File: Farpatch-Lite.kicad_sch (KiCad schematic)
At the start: 33 parts, among them J1 Program Header, J2 SWD Connector, SW1 Pushbutton 2.1x1.6mm, SW2 Pushbutton 2.1x1.6mm, U1 ‎ESP32-D0WD-V3‎, U2 Flash 32 Mb SPI, Y1 Crystal 40MHz

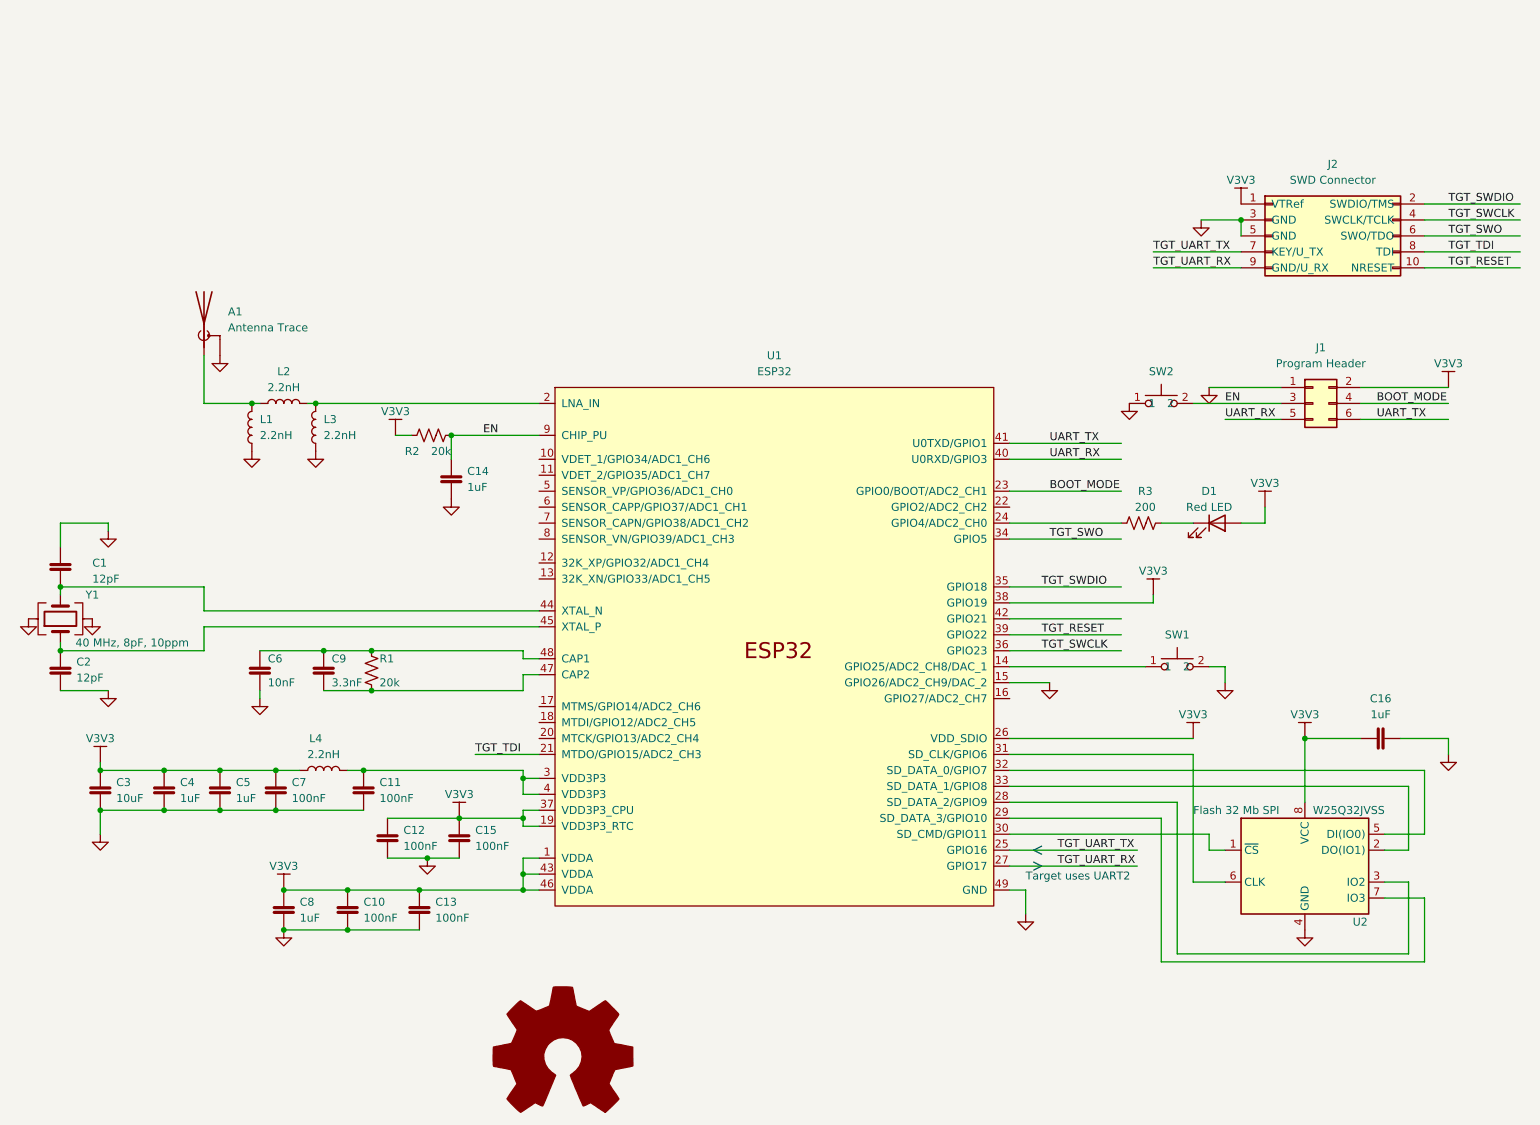
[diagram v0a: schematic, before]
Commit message: farpatch: finish layout and update README
Signed-off-by: Sean Cross <sean@xobs.io>
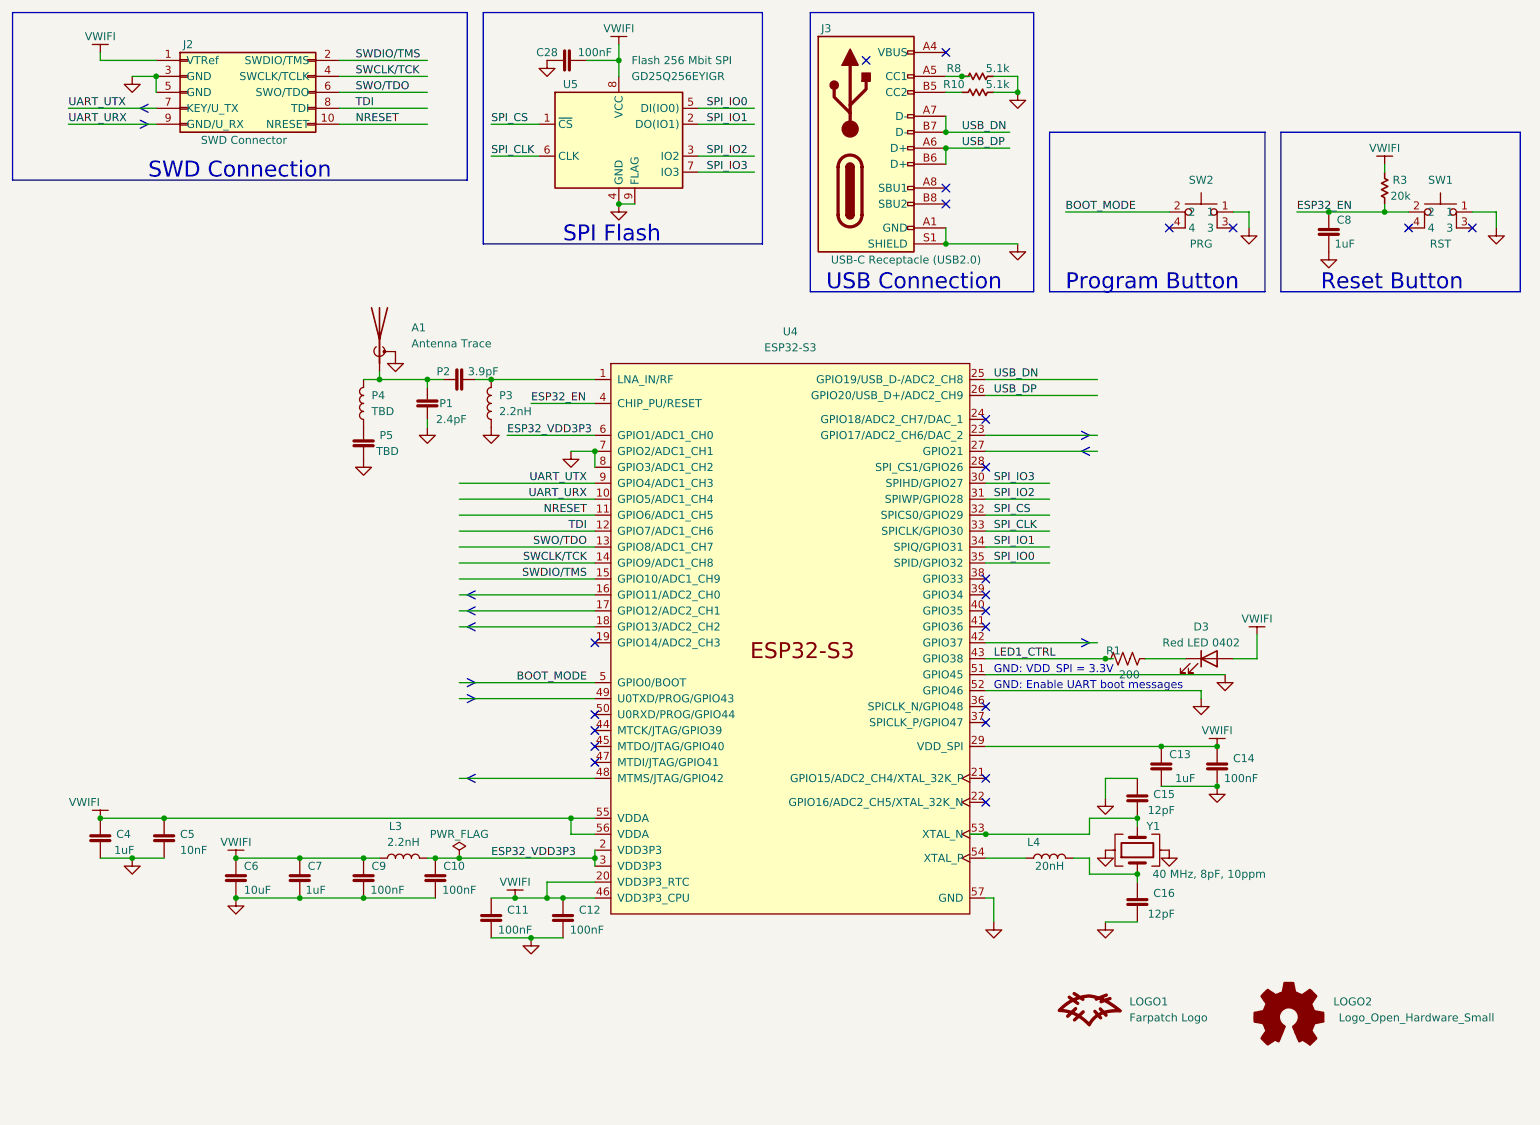
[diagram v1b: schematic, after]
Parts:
- removed C1, C2: Cap 12pF 0402, Capacitor_SMD:C_0402_1005Metric, symbol Farpatch-Lite:Cap 12pF 0402
- removed C13, C15, C7: Cap 100nF 0402, Capacitor_SMD:C_0402_1005Metric, symbol Farpatch-Lite:Cap 100nF 0402
- removed C14, C16, C5: Cap 1uF 0402, Capacitor_SMD:C_0402_1005Metric, symbol Farpatch-Lite:Cap 1uF 0402
- removed C3: Cap 10uF 0402, Capacitor_SMD:C_0402_1005Metric, symbol Farpatch-Lite:Cap 10uF 0402
- removed C6: Cap 10nF 0402, Capacitor_SMD:C_0402_1005Metric, symbol Farpatch-Lite:Cap 10nF 0402
- removed C9: Cap 3.3nF 0402, Capacitor_SMD:C_0402_1005Metric, symbol Farpatch-Lite:Cap 3.3nF 0402
- removed D1: Red LED, Farpatch-Lite:LED_0402_1005Metric, symbol Farpatch-Lite:Red LED
- removed J1: Program Header, Farpatch-Lite:PinHeader_2x03_P2.54mm_Vertical, symbol Farpatch-Lite:Program Header
- removed L1, L2, L3, L4: Ind 2.2nH 0402, Inductor_SMD:L_0402_1005Metric, symbol Farpatch-Lite:Ind 2.2nH 0402
- removed LOGO1: Logo_Open_Hardware_Large, Symbol:OSHW-Logo_5.7x6mm_SilkScreen, symbol Graphic:Logo_Open_Hardware_Large
- removed R1, R2: Res 20k 0402, Resistor_SMD:R_0402_1005Metric, symbol Farpatch-Lite:Res 20k 0402
- removed R3: Res 200 0402, Resistor_SMD:R_0402_1005Metric, symbol Farpatch-Lite:Res 200 0402
- removed SW1, SW2: Pushbutton 2.1x1.6mm, Farpatch-Lite:Pushbutton-2.1x1.6mm, symbol Farpatch-Lite:Pushbutton 2.1x1.6mm
- removed U1: ‎ESP32-D0WD-V3‎, Farpatch-Lite:QFN-48-1EP_5x5mm_P0.35mm_EP3.7x3.7mm_ThermalVias, symbol Farpatch-Lite:‎ESP32-D0WD-V3‎
- removed U2: Flash 32 Mb SPI, Farpatch-Lite:SOIC-8_5.23x5.23mm_P1.27mm, symbol Farpatch-Lite:Flash 32 Mb SPI
- added C13, C7: Cap 1uF 0402, Capacitor_SMD:C_0402_1005Metric, symbol Farpatch-Lite:Cap 1uF 0402
- added C14, C28, C9: Cap 100nF 0402, Capacitor_SMD:C_0402_1005Metric, symbol Farpatch-Lite:Cap 100nF 0402
- added C15, C16: Cap 12pF 0402, Capacitor_SMD:C_0402_1005Metric, symbol Farpatch-Lite:Cap 12pF 0402
- added C5: Cap 10nF 0402, Capacitor_SMD:C_0402_1005Metric, symbol Farpatch:Cap 10nF 0402
- added C6: Cap 10uF 0603, Capacitor_SMD:C_0603_1608Metric, symbol Farpatch:Cap 10uF 0603
- added D3: Red LED 0402, Farpatch-Lite:LED_0402_1005Metric, symbol Farpatch:Red LED 0402
- added J3: USB-C Receptacle (USB2.0), Farpatch-Lite:USB_C_Receptacle_HRO_TYPE-C-31-M-12, symbol Farpatch-Lite:USB-C Receptacle (USB2.0)
- added L3: L 2.2nH 0402, Inductor_SMD:L_0402_1005Metric, symbol Farpatch:L 2.2nH 0402
- added L4: L 20nH 0402, Inductor_SMD:L_0402_1005Metric, symbol Farpatch-Lite:L 20nH 0402
- added LOGO1: Farpatch Logo, Farpatch-Lite:Farpatch Logo, symbol Farpatch-Lite:Farpatch Logo
- added LOGO2: Logo_Open_Hardware_Small, Symbol:OSHW-Logo_5.7x6mm_SilkScreen, symbol Graphic:Logo_Open_Hardware_Small
- added P1: Cap 2.4pF 0402, Capacitor_SMD:C_0402_1005Metric, symbol Farpatch:Cap 2.4pF 0402
- added P2, P5: Cap 3.9pF 0402, Capacitor_SMD:C_0402_1005Metric, symbol Farpatch:Cap 3.9pF 0402
- added P3, P4: L 2.7 nH 0402, Inductor_SMD:L_0402_1005Metric, symbol Farpatch:L 2.7 nH 0402
- added R1: Res 200 0402, Resistor_SMD:R_0402_1005Metric, symbol Farpatch-Lite:Res 200 0402
- added R10, R8: R 5.1k 0402, Resistor_SMD:R_0402_1005Metric, symbol Farpatch:R 5.1k 0402
- added R3: Res 20k 0402, Resistor_SMD:R_0402_1005Metric, symbol Farpatch:R 20k 0402
- added SW1, SW2: Pushbutton 4.2x3.2mm 250gf, Farpatch-Lite:SW_SPST_PTS810, symbol Farpatch:Pushbutton 4.2x3.2mm 250gf
- added U4: ESP32-S3, Farpatch-Lite:QFN-56-1EP_7x7mm_P0.4mm_EP5.6x5.6mm_ThermalVias, symbol Farpatch-Lite:ESP32-S3
- added U5: Flash 256 Mbit SPI, Farpatch-Lite:WSON-8_8x6mm_P1.27mm, symbol Farpatch-Lite:Flash 256 Mbit SPI
- C11, C4: now in the parts list
- J2: footprint Farpatch-Lite:PinHeader_2x05_P1.27mm_Vertical_SMD -> Connector_PinHeader_1.27mm:PinHeader_2x05_P1.27mm_Vertical; Digikey (none) -> https://www.digikey.com/en/products/detail/cnc-tech/3220-10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
- Y1: value Crystal 40MHz -> Crystal 40MHz 2016
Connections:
- net BOOT_MODE: now also SW2.2, U4.5 (GPIO0/BOOT)
- net GND: now also C13.2, C14.2, C15.1, C16.2, C28.1, C5.2, C6.2, C7.2, C9.2, J3.A1 (GND), J3.A12 (GND), J3.B1 (GND), J3.B12 (GND), J3.S1 (SHIELD), P1.1, P3.1, P5.1, R10.2, R8.2, SW1.1, SW2.1, U4.51 (GPIO45), U4.52 (GPIO46), U4.57 (GND), U4.7 (GPIO2/ADC1_CH1), U4.8 (GPIO3/ADC1_CH2), U5.4 (GND), U5.9 (FLAG)
- net at Y1.1: now also C16.1, L4.2
- net at Y1.3: now also C15.2, U4.53 (XTAL_N)
- net VWIFI: now reaches C11.1
- net VWIFI: now also C12.1, C4.1, J2.1 (VTRef), C13.1, C14.1, C28.2, C5.1, C6.1, C7.1, C9.1, D3.2 (A), L3.1, R3.2, U4.20 (VDD3P3_RTC), U4.29 (VDD_SPI), U4.46 (VDD3P3_CPU), U4.55 (VDDA), U4.56 (VDDA), U5.8 (VCC)
- net at A1.1 (A): now also P1.2, P2.1, P4.2
- net TGT_RESET renamed NRESET
- net NRESET: now also U4.11 (GPIO6/ADC1_CH5)
- net TGT_SWCLK renamed SWCLK/TCK
- net SWCLK/TCK: now also U4.14 (GPIO9/ADC1_CH8)
- net TGT_SWDIO renamed SWDIO/TMS
- net SWDIO/TMS: now also U4.15 (GPIO10/ADC1_CH9)
- net TGT_SWO renamed SWO/TDO
- net SWO/TDO: now also U4.13 (GPIO8/ADC1_CH7)
- net TGT_TDI renamed TDI
- net TDI: now also U4.12 (GPIO7/ADC1_CH6)
- net TGT_UART_RX renamed UART_URX
- net UART_URX: now also U4.10 (GPIO5/ADC1_CH4)
- net TGT_UART_TX renamed UART_UTX
- net UART_UTX: now also U4.9 (GPIO4/ADC1_CH3)
- removed net V3V3: C10.1, C12.1, C4.1, C8.1, J2.1 (VTRef)
- new net: P2.2, P3.2, U4.1 (LNA_IN/RF)
- new net: D3.1 (K), R1.2
- new net: J3.B5 (CC2), R10.1
- new net: L4.1, U4.54 (XTAL_P)
- new net: P4.1, P5.2
- new net: J3.A4 (VBUS), J3.B9 (VBUS)
- new net: J3.A5 (CC1), R8.1
- new net: J3.A9 (VBUS), J3.B4 (VBUS)
- new net ESP32_EN: C8.1, R3.1, SW1.2, U4.4 (CHIP_PU/RESET)
- new net ESP32_VDD3P3: C10.1, L3.2, U4.2 (VDD3P3), U4.3 (VDD3P3), U4.6 (GPIO1/ADC1_CH0)
- new net LED1_CTRL: R1.1, U4.43 (GPIO38)
- new net SPI_CLK: U4.33 (SPICLK/GPIO30), U5.6 (CLK)
- new net SPI_CS: U4.32 (SPICS0/GPIO29), U5.1 (~{CS})
- new net SPI_IO0: U4.35 (SPID/GPIO32), U5.5 (DI(IO0))
- new net SPI_IO1: U4.34 (SPIQ/GPIO31), U5.2 (DO(IO1))
- new net SPI_IO2: U4.31 (SPIWP/GPIO28), U5.3 (IO2)
- new net SPI_IO3: U4.30 (SPIHD/GPIO27), U5.7 (IO3)
- new net USB_DN: J3.A7 (D-), J3.B7 (D-), U4.25 (GPIO19/USB_D-/ADC2_CH8)
- new net USB_DP: J3.A6 (D+), J3.B6 (D+), U4.26 (GPIO20/USB_D+/ADC2_CH9)
- no-connect marks 0 -> 23
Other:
- note added: "GND: Enable UART boot messages"
- note added: "GND: VDD_SPI = 3.3V"
- note added: "Program Button"
- note added: "Reset Button"
- note added: "SPI Flash"
- note added: "SWD Connection"
- note added: "USB Connection"
- note removed: "Target uses UART2"
- company: (none) -> Foosn PTE Ltd
- title: (none) -> Farpatch Main
